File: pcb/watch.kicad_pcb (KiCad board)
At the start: 2 copper layers, 31 x 39 mm, 2 parts, among them J1 USB_C_Receptacle_USB2.0_16P, U1 ESP32-S3-WROOM-1

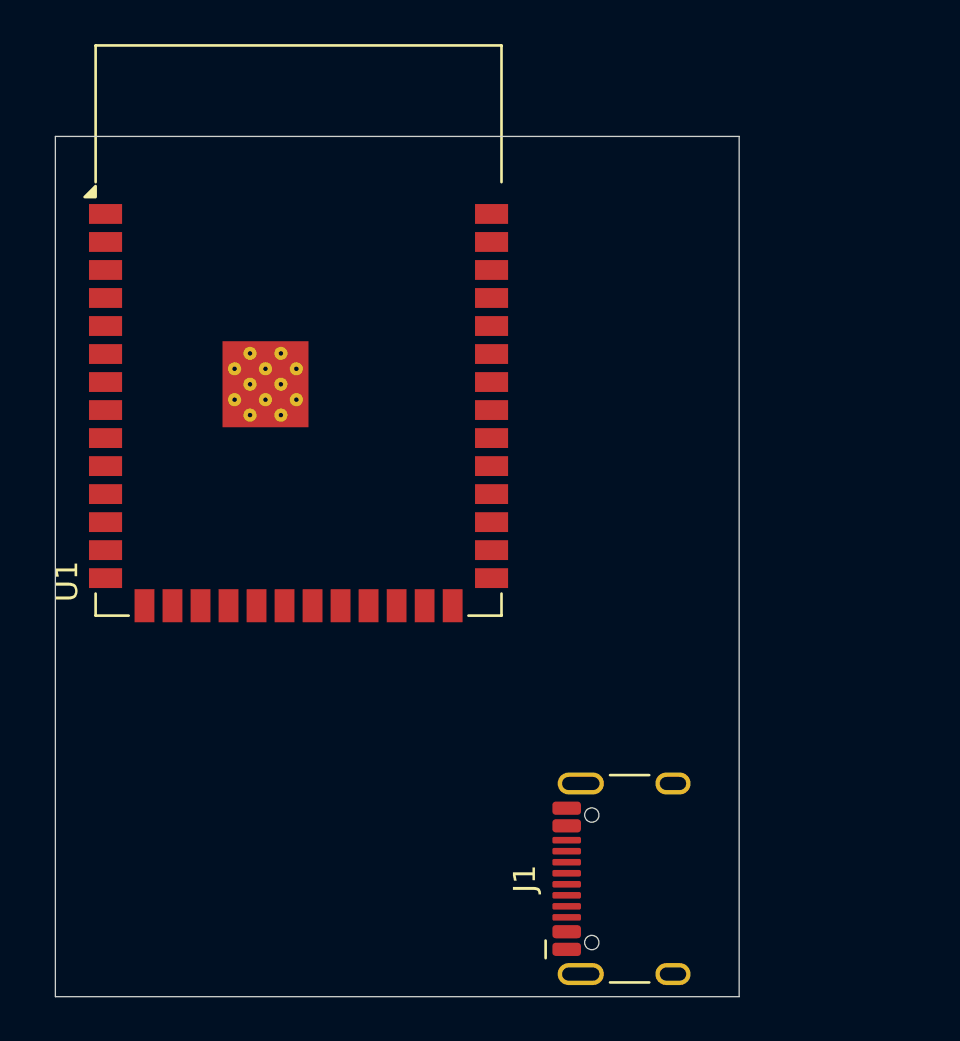
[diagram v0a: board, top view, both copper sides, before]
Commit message: Placing the PCB correctly, replacing ESP32-S3-WROOM-1 by ESP32-S3-WROOM-1U, placing AMS1117
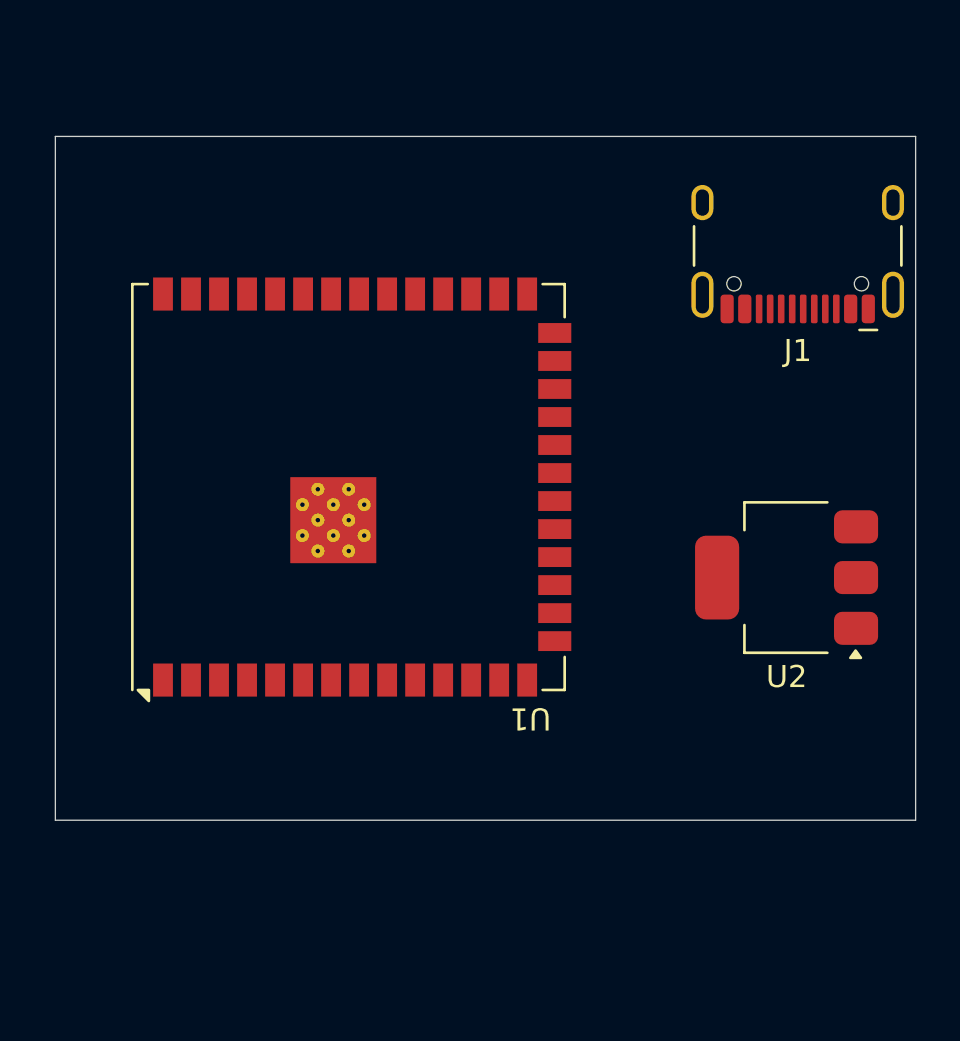
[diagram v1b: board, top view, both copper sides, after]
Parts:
- added U2: AMS1117-3.3, Package_TO_SOT_SMD:SOT-223-3_TabPin2, F.Cu at (153.2, 90.0)
- U1: footprint RF_Module:ESP32-S3-WROOM-1 -> RF_Module:ESP32-S3-WROOM-1U
- moved J1 30.3 mm to (153.7, 74.1), turned to 180 degrees
- moved U1 7.47 mm to (133.3, 85.9), turned to 90 degrees
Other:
- board size 31 x 39 mm -> 39 x 31 mm
